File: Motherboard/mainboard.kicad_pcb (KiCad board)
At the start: 4 copper layers, 35 x 35 mm, 39 parts, among them IC1 BMX160, J1 Conn_01x01, J2 10118194-0001LF, J28 Conn_01x01, J29 Conn_01x01, J3 Micro_SD_Card, J30 Conn_01x01, J4 xf2m-2415-1a, J5 XF2M-1015-1A, J6 Conn_01x02, SW1 KMR231NG LFS, U1 RFM95W-915S2, U2 ATSAMD51G_TQFN48, U3 DRV8833PWP, U4 TPS82740BSIPR, U5 DRV8833PWP, U6 MAX708RESA-T, U8 RFM95W-915S2, X1 ANTENNA_U.FL, X2 ANTENNA_U.FL

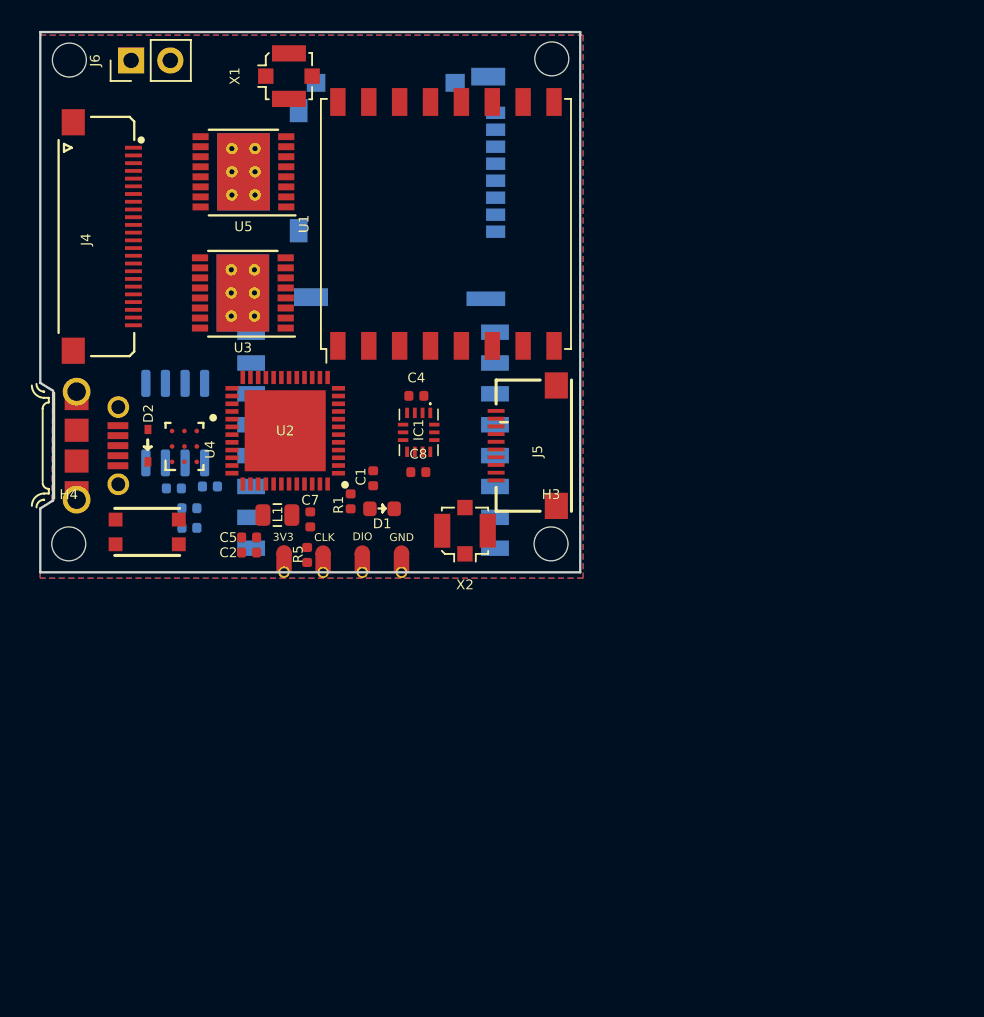
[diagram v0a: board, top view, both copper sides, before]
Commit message: updated PCB layout
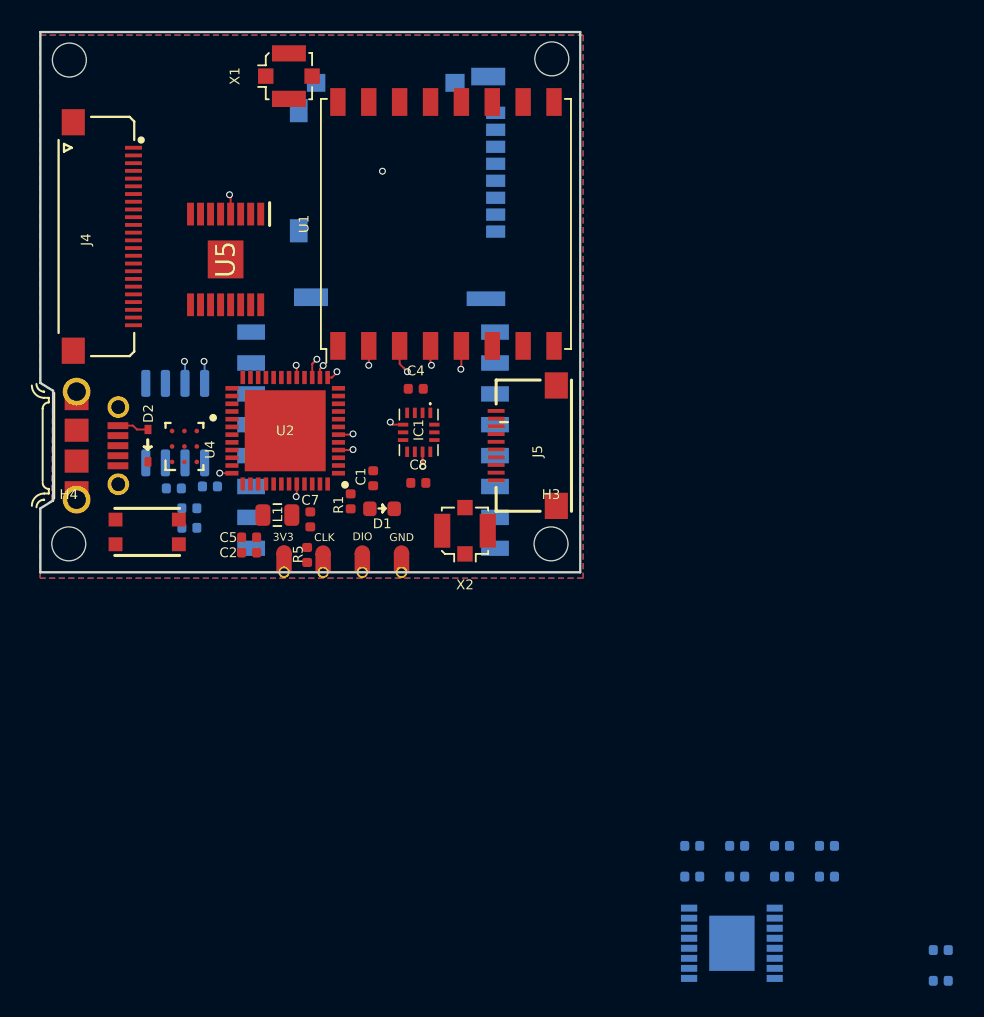
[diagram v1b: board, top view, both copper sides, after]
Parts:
- removed J6: Conn_01x02, Connector_PinHeader_2.54mm:PinHeader_1x02_P2.54mm_Vertical
- added C10: 10uF, Capacitor_SMD:C_0402_1005Metric, B.Cu at (126.9, 128.8)
- added C11: 2.2uF, Capacitor_SMD:C_0402_1005Metric, B.Cu at (124.0, 126.8)
- added C12: 0.1uF, Capacitor_SMD:C_0402_1005Metric, B.Cu at (140.1, 135.5)
- added C13: 2.2uF, Capacitor_SMD:C_0402_1005Metric, B.Cu at (126.9, 126.8)
- added C14: 10uF, Capacitor_SMD:C_0402_1005Metric, B.Cu at (129.8, 128.8)
- added C9: 0.1uF, Capacitor_SMD:C_0402_1005Metric, B.Cu at (124.0, 128.8)
- added R4: 10K, Resistor_SMD:R_0402_1005Metric, B.Cu at (140.1, 133.5)
- added R6: 10K, Resistor_SMD:R_0402_1005Metric, B.Cu at (132.7, 128.8)
- added R7: 10K, Resistor_SMD:R_0402_1005Metric, B.Cu at (129.8, 126.8)
- added R8: 10K, Resistor_SMD:R_0402_1005Metric, B.Cu at (132.7, 126.8)
- U3: value DRV8833PWP -> DRV8848; footprint Package_SO:HTSSOP-16-1EP_4.4x5mm_P0.65mm_EP3.4x5mm_Mask2.46x2.31mm_ThermalVias -> Package_SO:TSSOP-16-1EP_4.4x5mm_P0.65mm; moved to B.Cu
- U5: value DRV8833PWP -> DRV8848; footprint Package_SO:HTSSOP-16-1EP_4.4x5mm_P0.65mm_EP3.4x5mm_Mask2.46x2.31mm_ThermalVias -> KiCAD Libraries:SOP65P640X120-17N
- moved U3 52.7 mm to (126.5, 133.1), turned to 0 degrees
- moved U5 5.79 mm to (93.7, 88.8), turned to 270 degrees
- moved C8 0.70 mm to (106.2, 103.3)
- moved C4 0.46 mm to (106.0, 97.2)
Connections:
- net Net-(J4-Pad1) renamed 3V3
- net Net-(J4-Pad10) renamed COIL3P
- net Net-(J4-Pad11) renamed BURN2
- net Net-(J4-Pad12) renamed COIL3N
- net Net-(J4-Pad2) renamed COIL1P
- net Net-(J4-Pad4) renamed COIL1N
- net Net-(J4-Pad6) renamed COIL2P
- net Net-(J4-Pad8) renamed COIL2N
- net Net-(J4-Pad9) renamed BURN1
- J4 pad 13: Net-(J4-Pad13) -> SCL1
- J4 pad 14: Net-(J4-Pad14) -> SCL2
- J4 pad 15: Net-(J4-Pad15) -> SDA1
- J4 pad 16: Net-(J4-Pad16) -> SDA2
- J4 pad 3: Net-(J4-Pad3) -> GND
- J4 pad 5: Net-(J4-Pad5) -> BATT_P
- J4 pad 7: Net-(J4-Pad7) -> BATT_N
- J5 pad 1: Net-(J5-Pad1) -> BATT_P
- J5 pad 10: Net-(J5-Pad10) -> EN_CAM
- J5 pad 2: Net-(J5-Pad2) -> GND
- J5 pad 3: Net-(J5-Pad3) -> MOSI
- J5 pad 4: Net-(J5-Pad4) -> BATT_N
- J5 pad 5: Net-(J5-Pad5) -> CS_CAM
- J5 pad 7: Net-(J5-Pad7) -> MISO
- J5 pad 9: Net-(J5-Pad9) -> SCK
- U2 pad 1: RF_BUSY -> SDA1
- U2 pad 2: RF_DIO3 -> SCL1
- U2 pad 22: Net-(U2-Pad22) -> RF_BUSY
- U2 pad 23: Net-(U2-Pad23) -> RF_DIO3
- U2 pad 24: Net-(U2-Pad24) -> CS_CAM
- U2 pad 25: SDA -> SCL2
- U2 pad 26: SCL -> SDA2
- U2 pad 29: Net-(U2-Pad29) -> EN_CAM
- U3 pad 1: Net-(U3-Pad1) -> MXZ_EN
- U3 pad 10: Net-(U3-Pad10) -> MINZ_2
- U3 pad 11: Net-(U3-Pad11) -> VINT_1
- U3 pad 13: Net-(U3-Pad13) -> GND
- U3 pad 15: Net-(U3-Pad15) -> MINX_2
- U3 pad 16: Net-(U3-Pad16) -> MINX_1
- U3 pad 17: Net-(U3-Pad17) -> GND
- U3 pad 2: Net-(U3-Pad2) -> MINX_1
- U3 pad 3: Net-(U3-Pad3) -> GND
- U3 pad 4: Net-(U3-Pad4) -> MINX_2
- U3 pad 5: Net-(U3-Pad5) -> MOZ_2
- U3 pad 6: Net-(U3-Pad6) -> GND
- U3 pad 7: Net-(U3-Pad7) -> MOZ_1
- U3 pad 8: Net-(U3-Pad8) -> DXZ_FAULT
- U3 pad 9: Net-(U3-Pad9) -> MINZ_1
- U5 pad 1: Net-(U5-Pad1) -> MXZ_EN
- U5 pad 10: Net-(U5-Pad10) -> MINZ_2
- U5 pad 11: Net-(U5-Pad11) -> VINT_1
- U5 pad 13: Net-(U5-Pad13) -> GND
- U5 pad 15: Net-(U5-Pad15) -> MINX_2
- U5 pad 16: Net-(U5-Pad16) -> MINX_1
- U5 pad 17: Net-(U5-Pad17) -> GND
- U5 pad 2: Net-(U5-Pad2) -> MINX_1
- U5 pad 3: Net-(U5-Pad3) -> GND
- U5 pad 4: Net-(U5-Pad4) -> MINX_2
- U5 pad 5: Net-(U5-Pad5) -> MOZ_2
- U5 pad 6: Net-(U5-Pad6) -> GND
- U5 pad 7: Net-(U5-Pad7) -> MOZ_1
- U5 pad 8: Net-(U5-Pad8) -> DXZ_FAULT
- U5 pad 9: Net-(U5-Pad9) -> MINZ_1
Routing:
- net Net-(IC1-Pad10): track 0.00 -> 36.4 mm, vias 0 -> 2
- net SCK: track 0.00 -> 9.68 mm, vias 0 -> 2
- net (no net): track 0.00 -> 9.53 mm
- net MOSI: track 0.00 -> 7.49 mm, vias 0 -> 2
- net MISO: track 0.00 -> 6.67 mm, vias 0 -> 2
- net MINX_2: track 0.00 -> 6.59 mm, vias 0 -> 1
- net +3V3: track 0.00 -> 5.25 mm, vias 0 -> 6
- net GND: track 0.00 -> 2.88 mm, vias 0 -> 2
- net VUSB: track 0.00 -> 2.05 mm
- net CS_RF2: track 0.00 -> 1.53 mm, vias 0 -> 1
